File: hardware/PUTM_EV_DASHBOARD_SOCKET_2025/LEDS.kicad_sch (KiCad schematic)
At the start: 15 parts, among them Q4 BSS138, Q5 BSS138, Q6 BSS138

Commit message: prawie gotowe
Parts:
- renumbered D10 to AMS0, D12 to FUSE_LED0, D11 to SAFETY_LED0
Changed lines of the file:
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@@
 		(on_board yes)
 		(dnp no)
-		(property "Reference" "D10"
+		(property "Reference" "AMS0"
 			(at 144.78 86.36 90)
 			(effects
@@
 			(project "PUTM_EV_DASHBOARD_SOCKET_2025"
 				(path "/8dcb9295-4fa2-433e-bd2f-4b006d008a4e/3b3cf35a-a2ef-483a-8c57-15009dc39242"
-					(reference "D10")
+					(reference "AMS0")
 					(unit 1)
 				)
@@
 		(on_board yes)
 		(dnp no)
-		(property "Reference" "D11"
+		(property "Reference" "SAFETY_LED0"
 			(at 99.06 86.36 90)
 			(effects
@@
 			(project "PUTM_EV_DASHBOARD_SOCKET_2025"
 				(path "/8dcb9295-4fa2-433e-bd2f-4b006d008a4e/3b3cf35a-a2ef-483a-8c57-15009dc39242"
-					(reference "D11")
+					(reference "SAFETY_LED0")
 					(unit 1)
 				)
@@
 		(on_board yes)
 		(dnp no)
-		(property "Reference" "D12"
+		(property "Reference" "FUSE_LED0"
 			(at 55.88 86.36 90)
 			(effects
@@
 			(project "PUTM_EV_DASHBOARD_SOCKET_2025"
 				(path "/8dcb9295-4fa2-433e-bd2f-4b006d008a4e/3b3cf35a-a2ef-483a-8c57-15009dc39242"
-					(reference "D12")
-					(unit 1)
-				)
+					(reference "FUSE_LED0")
+					(unit 1)
+				)

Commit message: jest jako tako
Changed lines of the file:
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@@
 		)
 	)
-	(global_label "SAFETY_LED"
+	(hierarchical_label "FUSE_LED"
 		(shape input)
-		(at 76.2 96.52 180)
-		(fields_autoplaced yes)
+		(at 33.02 96.52 180)
 		(effects
 			(font
@@
 			(justify right)
 		)
-		(property "Intersheetrefs" "${INTERSHEET_REFS}"
-			(at 62.2082 96.52 0)
-			(effects
-				(font
-					(size 1.27 1.27)
-				)
-				(justify right)
-				(hide yes)
-			)
-		)
 	)
-	(global_label "AMS"
+	(hierarchical_label "AMS"
 		(shape input)
 		(at 121.92 96.52 180)
-		(fields_autoplaced yes)
 		(effects
 			(font
@@
 			(justify right)
 		)
-		(property "Intersheetrefs" "${INTERSHEET_REFS}"
-			(at 115.1853 96.52 0)
-			(effects
-				(font
-					(size 1.27 1.27)
-				)
-				(justify right)
-				(hide yes)
-			)
-		)
 	)
-	(global_label "FUSE_LED"
+	(hierarchical_label "SAFETY_LED"
 		(shape input)
-		(at 33.02 96.52 180)
-		(fields_autoplaced yes)
+		(at 76.2 96.52 180)
 		(effects
 			(font
@@
 			(justify right)
 		)
-		(property "Intersheetrefs" "${INTERSHEET_REFS}"
-			(at 20.8425 96.52 0)
-			(effects
-				(font
-					(size 1.27 1.27)
-				)
-				(justify right)
-				(hide yes)
-			)
-		)
 	)

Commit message: g3
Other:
- note added: "LEDY"
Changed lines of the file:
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@@
 	(generator_version "9.0")
 	(paper "A4")
+	(rectangle
+		(start 17.145 55.245)
+		(end 156.21 118.11)
+		(stroke
+			(width 0)
+			(type default)
+		)
+		(fill
+			(type none)
+		)
+	)
 	(text "100 mW"
 		(exclude_from_sim no)
@@
 		(effects
 			(font
+				(size 1.27 1.27)
+			)
+		)
+	)
+	(text "LEDY\n"
+		(exclude_from_sim no)
+		(at 37.846 60.706 0)
+		(effects
+			(font

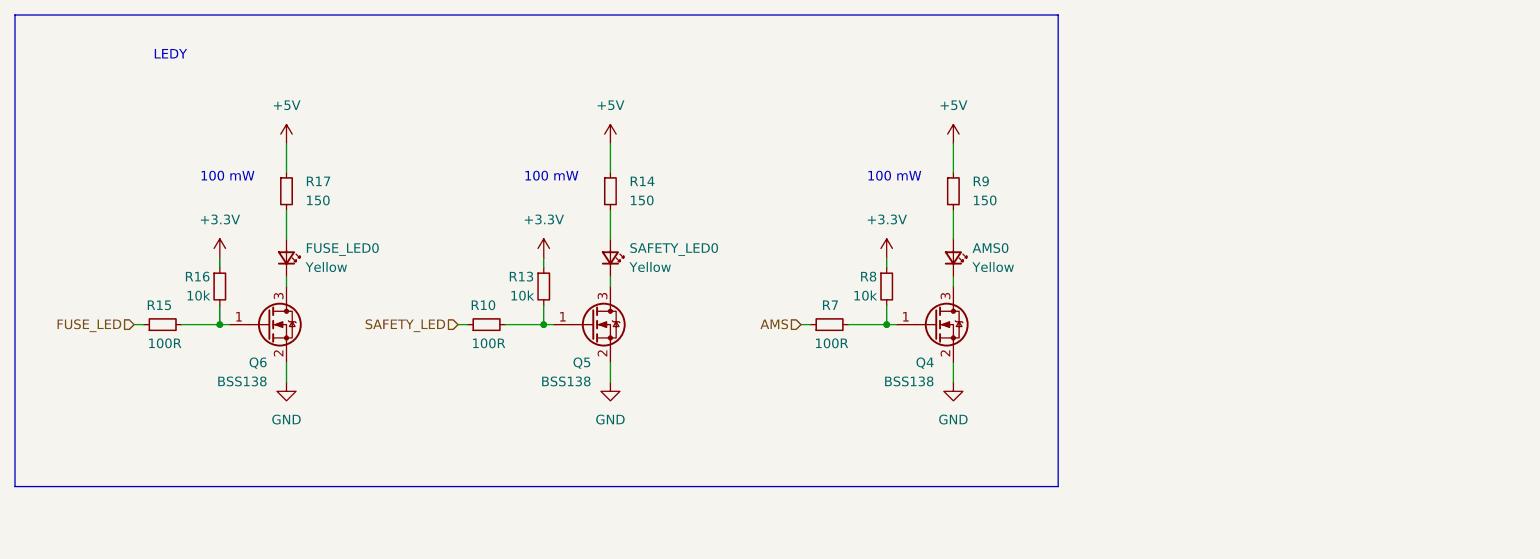
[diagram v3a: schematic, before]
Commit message: fixed button logic, holes for inserts, distance from mounting holes to P4 socket, changed jumpers, TVS diode and footprint for laboratory socket 4m
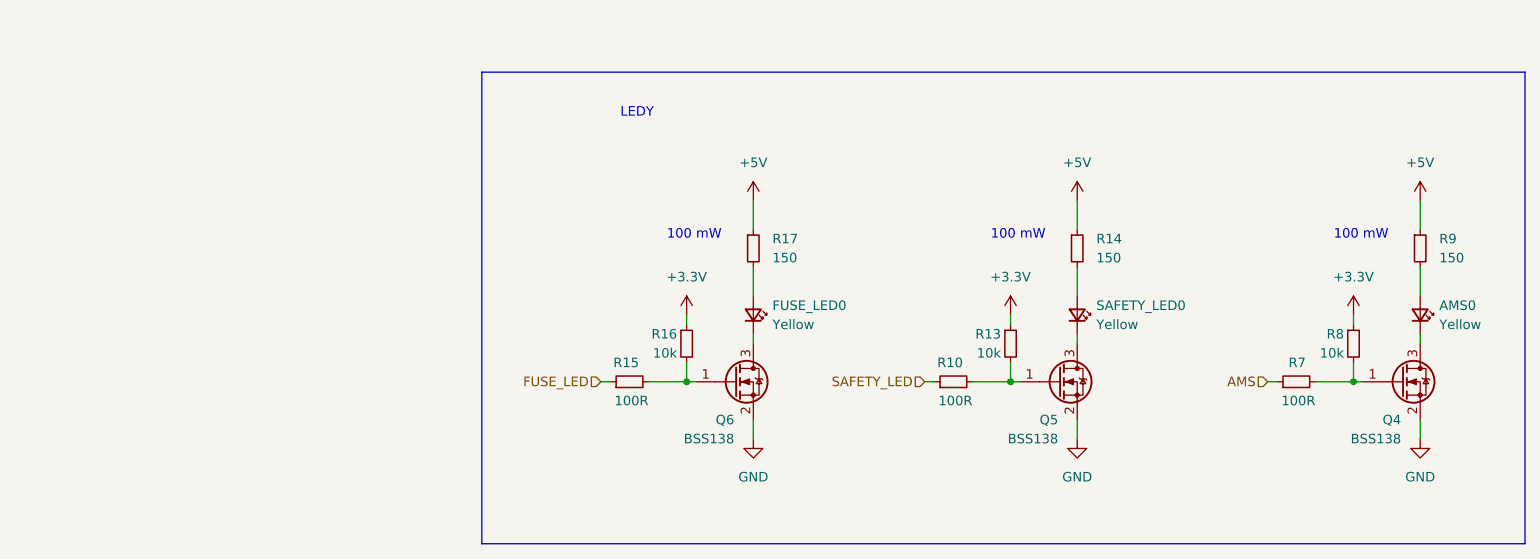
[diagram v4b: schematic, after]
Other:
- moved on the sheet: AMS0, FUSE_LED0, Q4, Q5, Q6, R10, R13, R14, R15, R16, R17, R7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
